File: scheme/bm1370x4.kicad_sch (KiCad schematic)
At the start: 87 parts, among them J2 Conn_01x04, U19 BM1370_mode1, U2 TMUX1109RSVR, U20 BM1370_mode1, U25 BM1370_mode1, U26 BM1370_mode1, U35 TXU0304PW, U5 TMP451, U8 25MHz

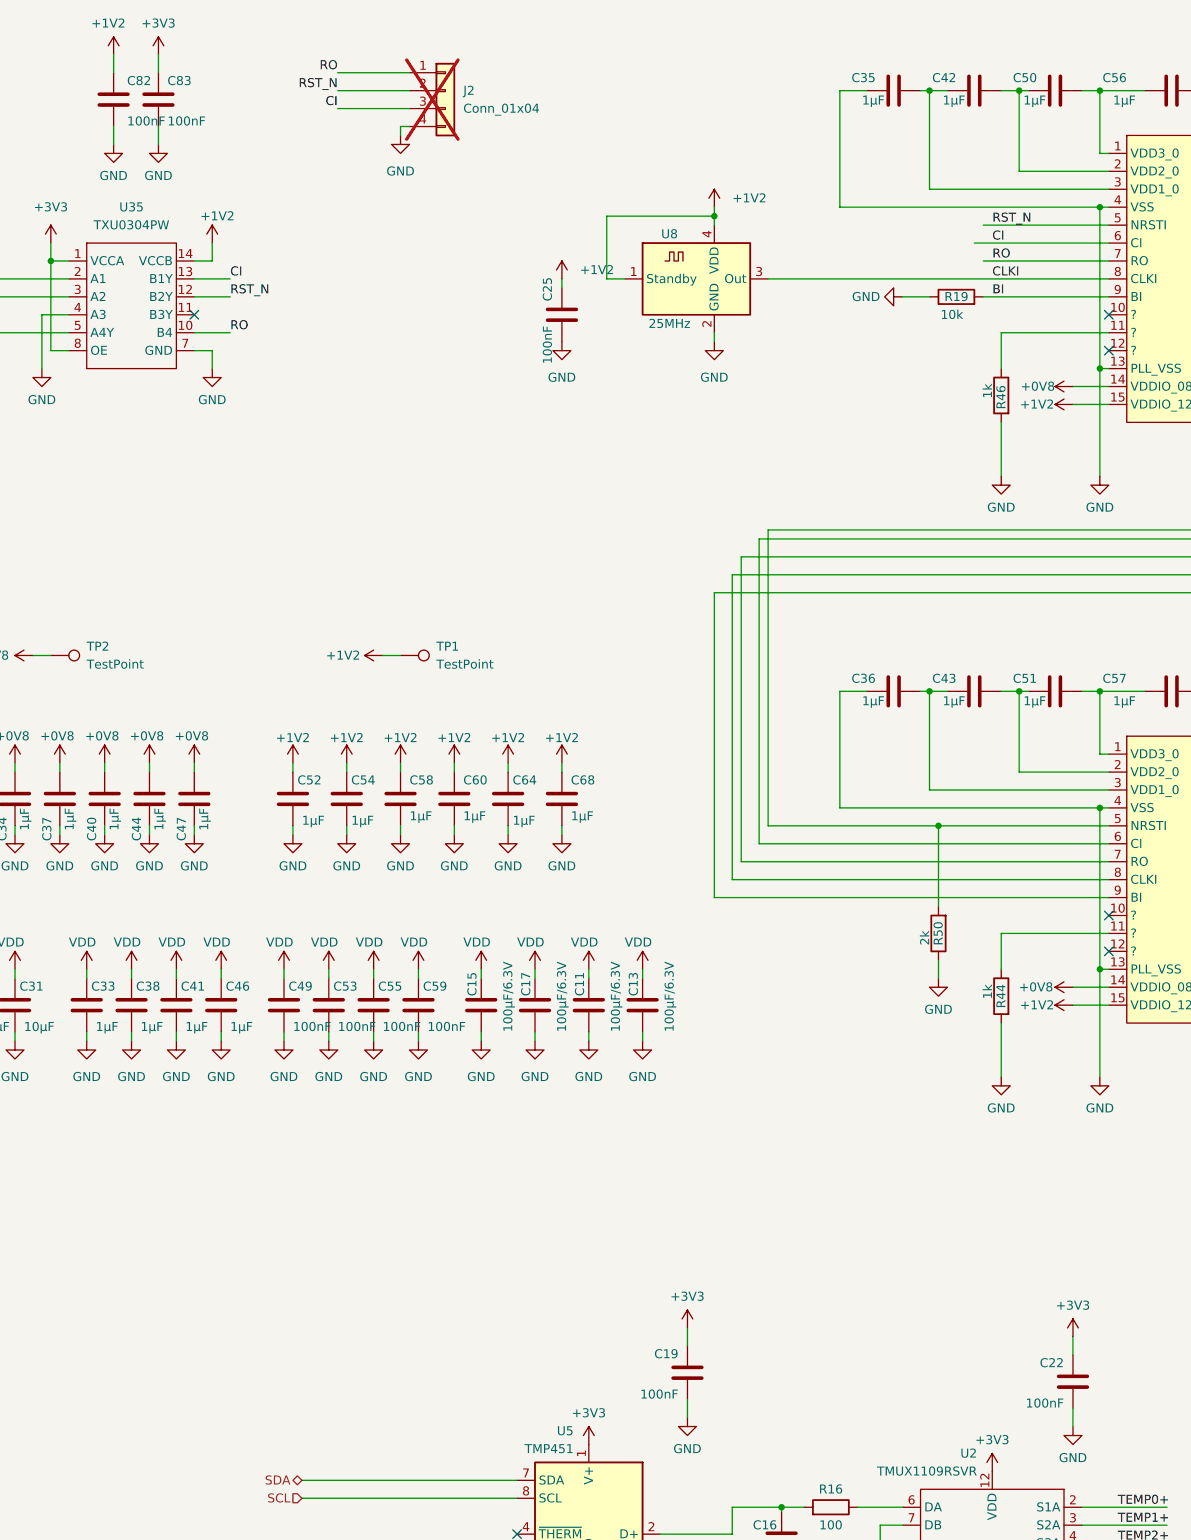
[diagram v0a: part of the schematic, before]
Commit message: Updated schematics with correct cap rating
We upgraded certain capacitors to a higher nF rating and have changed the schematic to reflect it so the BOM can be generated accurately.
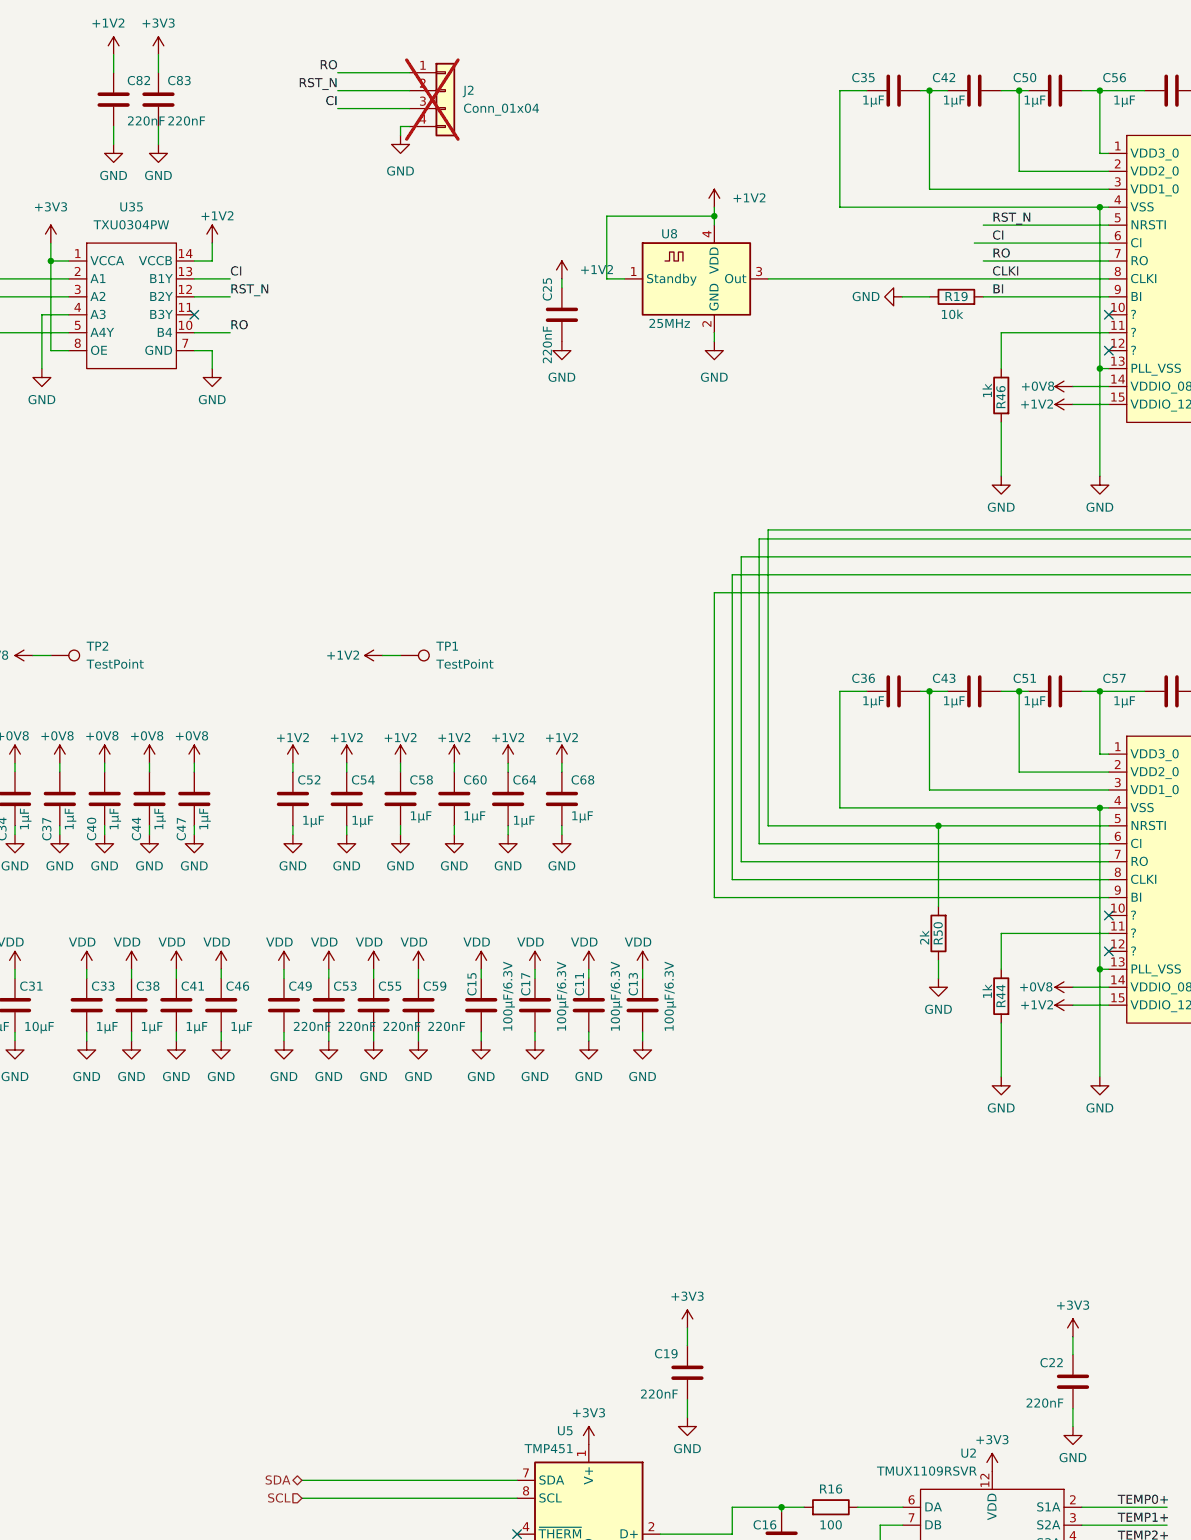
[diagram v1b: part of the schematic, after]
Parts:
- C19, C22, C25, C49, C53, C55, C59, C82, C83: value 100nF -> 220nF
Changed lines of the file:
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@@
 			)
 		)
-		(property "Value" "100nF"
+		(property "Value" "220nF"
 			(at 82.55 158.75 0)
 			(effects
@@
 			)
 		)
-		(property "Value" "100nF"
+		(property "Value" "220nF"
 			(at 191.77 212.09 0)
 			(effects
@@
 			)
 		)
-		(property "Value" "100nF"
+		(property "Value" "220nF"
 			(at 64.77 30.48 0)
 			(effects
@@
 			)
 		)
-		(property "Value" "100nF"
+		(property "Value" "220nF"
 			(at 88.9 158.75 0)
 			(effects
@@
 			)
 		)
-		(property "Value" "100nF"
+		(property "Value" "220nF"
 			(at 119.38 64.135 90)
 			(effects
@@
 			)
 		)
-		(property "Value" "100nF"
+		(property "Value" "220nF"
 			(at 101.6 158.75 0)
 			(effects
@@
 			)
 		)
-		(property "Value" "100nF"
+		(property "Value" "220nF"
 			(at 137.16 210.82 0)
 			(effects
@@
 			)
 		)
-		(property "Value" "100nF"
+		(property "Value" "220nF"
 			(at 59.055 30.48 0)
 			(effects
@@
 			)
 		)
-		(property "Value" "100nF"
+		(property "Value" "220nF"
 			(at 95.25 158.75 0)
 			(effects
